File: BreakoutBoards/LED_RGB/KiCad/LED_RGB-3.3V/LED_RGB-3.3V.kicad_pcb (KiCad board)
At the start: 2 copper layers, 11.8 x 12.6 mm, 1 part

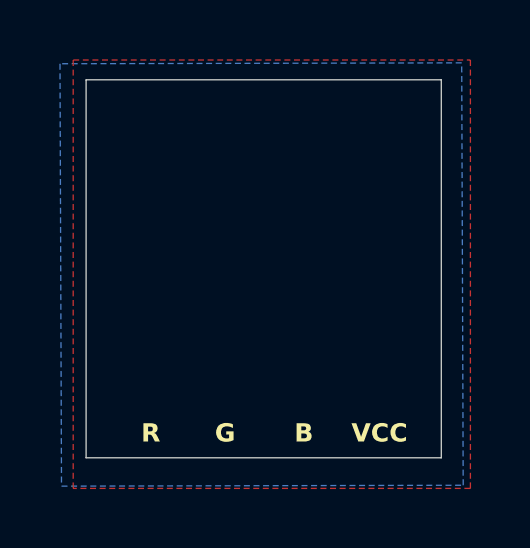
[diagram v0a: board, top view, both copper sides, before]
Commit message: updated to Mk1 and sent for manufacturing
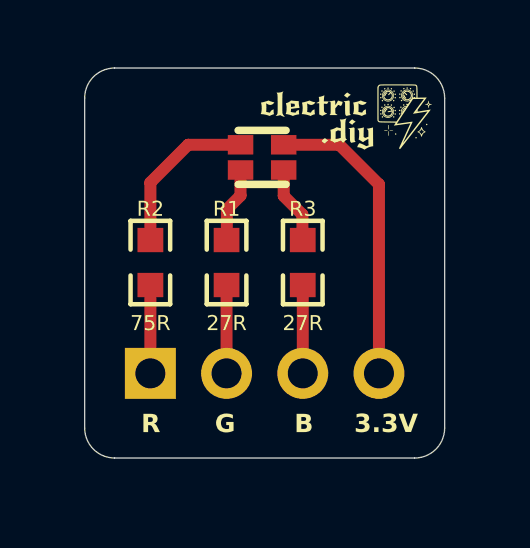
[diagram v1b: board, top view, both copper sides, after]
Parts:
- removed the G*** at (94.7, 81.3)
- added G***: LOGO, LOGO, F.Cu at (97.4, 80.1)
- added G***: LOGO, LOGO, B.Cu at (94.7, 81.0)
- added J1: Connector_PinHeader_2.54mm, Connector_PinHeader_2.54mm:PinHeader_1x04_P2.54mm_Vertical, B.Cu at (90.9, 88.6)
- added R1: 27R, clectric-diy:R0603, F.Cu at (93.5, 85.0)
- added R2: 75R, clectric-diy:R0603, F.Cu at (90.9, 85.0)
- added R3: 27R, clectric-diy:R0603, F.Cu at (96.0, 85.0)
- added U1: A-SP1943B1GHR6C-C01-2T, clectric-diy:LED-SMD_4P-L1.6-W1.5-BL_A-SP1943B1GHR6C-C01-2T, F.Cu at (94.7, 81.4)
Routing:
- net 3.3V: track 0.00 -> 10.0 mm
- net LED_RED: track 0.00 -> 8.39 mm
- net LED_BLUE: track 0.00 -> 5.54 mm
- net LED_GREEN: track 0.00 -> 5.47 mm
- removed copper zone on B.Cu, net GND
- removed copper zone on F.Cu, net GND
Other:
- board size 11.8 x 12.6 mm -> 12 x 13 mm
- board text added: "3.3V"
- board text added: "Charge 3.3V RGB LED"
- board text added: "LED: A-SP1943B1GHR6C-C01-2T"
- board text removed: "Charge LED_RGB Mk 0.1"
- board text removed: "VCC"
